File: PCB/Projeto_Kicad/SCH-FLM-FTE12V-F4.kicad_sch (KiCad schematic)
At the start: 19 parts, among them J1 BPSC-4, J2 MCS-6, Q3 BC547, Q4 BC547, U1 ESP32-WROOM-32E-N8, U2 LM358N

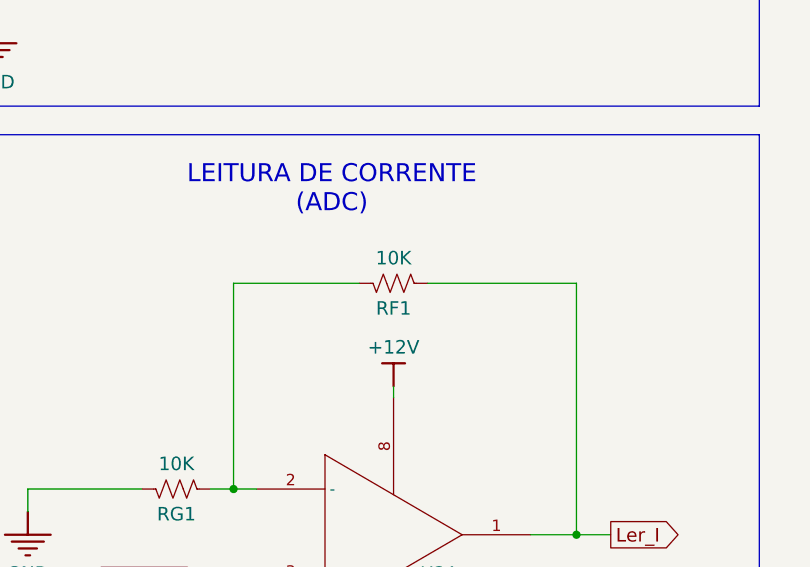
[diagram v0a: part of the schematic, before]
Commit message: Adição do R7 em paralelo com R6 e adição do RF2 de 15K e mudança de valor do RF1 de 10K para 15K
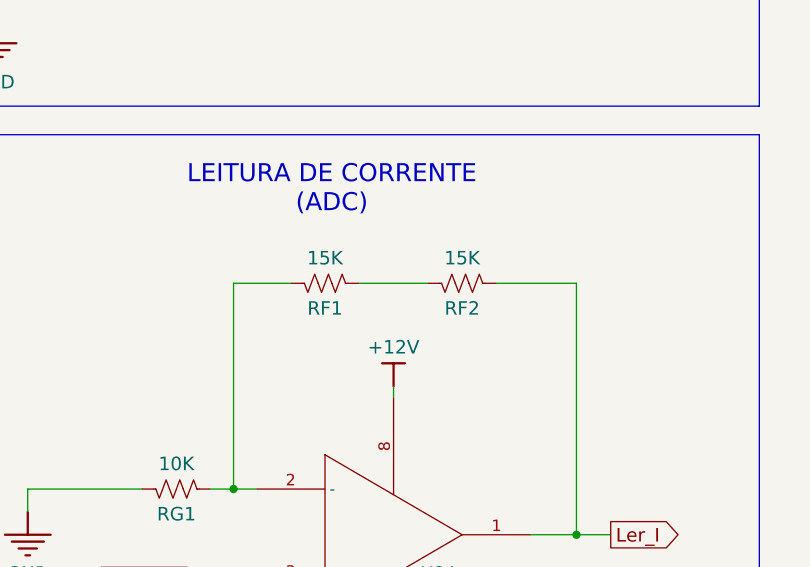
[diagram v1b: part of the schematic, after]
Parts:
- added RF2: 15K, Resistor_THT:R_Axial_DIN0207_L6.3mm_D2.5mm_P2.54mm_Vertical, symbol Device:R_US
- RF1: value 10K -> 15K
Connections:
- net Ler_I: now also RF2.2; no longer RF1.2
- new net: RF1.2, RF2.1
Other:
- moved on the sheet: RF1
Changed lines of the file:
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@@
+	(wire
+		(pts
+			(xy 120.65 227.33) (xy 129.54 227.33)
+		)
+		(stroke
+			(width 0)
+			(type default)
+		)
+	)
 	(wire
 		(pts
@@
 	(wire
 		(pts
-			(xy 105.41 227.33) (xy 91.44 227.33)
+			(xy 97.79 227.33) (xy 91.44 227.33)
 		)
 		(stroke
@@
 	(wire
 		(pts
-			(xy 113.03 227.33) (xy 129.54 227.33)
-		)
-		(stroke
-			(width 0)
-			(type default)
-		)
-	)
-	(wire
-		(pts
 			(xy 81.28 250.19) (xy 68.58 250.19)
 		)
@@
 		(pts
 			(xy 55.88 58.42) (xy 69.85 58.42)
+		)
+		(stroke
+			(width 0)
+			(type default)
+		)
+	)
+	(wire
+		(pts
+			(xy 105.41 227.33) (xy 113.03 227.33)
 		)
 		(stroke
@@
 				(path "/24c863d3-5da9-46c2-adf2-885da2a6f9d5/d196a6d6-d89b-4d92-bbb9-3bc0a8b87648"
 					(reference "R9")
+					(unit 1)
+				)
+			)
+		)
+	)
+	(symbol
+		(lib_id "Device:R_US")
+		(at 116.84 227.33 90)
+		(mirror x)
+		(unit 1)
+		(body_style 1)
+		(exclude_from_sim no)
+		(in_bom yes)
+		(on_board yes)
+		(in_pos_files yes)
+		(dnp no)
+		(property "Reference" "RF2"
+			(at 116.84 230.124 90)
+			(show_name no)
+			(do_not_autoplace no)
+			(effects
+				(font
+					(size 1.5 1.5)
+				)
+			)
+		)
+		(property "Value" "15K"
+			(at 116.84 224.536 90)
+			(show_name no)
+			(do_not_autoplace no)
+			(effects
+				(font
+					(size 1.5 1.5)
+				)
+			)
+		)
+		(property "Footprint" "Resistor_THT:R_Axial_DIN0207_L6.3mm_D2.5mm_P2.54mm_Vertical"
+			(at 117.094 228.346 90)
+			(hide yes)
+			(show_name no)
+			(do_not_autoplace no)
+			(effects
+				(font
+					(size 1.27 1.27)
+				)
+			)
+		)
+		(property "Datasheet" ""
+			(at 116.84 227.33 0)
+			(hide yes)
+			(show_name no)
+			(do_not_autoplace no)
+			(effects
+				(font
+					(size 1.27 1.27)
+				)
+			)
+		)
+		(property "Description" "Resistor, US symbol"
+			(at 116.84 227.33 0)
+			(hide yes)
+			(show_name no)
+			(do_not_autoplace no)
+			(effects
+				(font
+					(size 1.27 1.27)
+				)
+			)
+		)
+		(pin "1"
+		)
+		(pin "2"
+		)
+		(instances
+			(project "PCB-FLM-FTE-12V"
+				(path "/24c863d3-5da9-46c2-adf2-885da2a6f9d5/d196a6d6-d89b-4d92-bbb9-3bc0a8b87648"
+					(reference "RF2")
 					(unit 1)
 				)
@@
 	(symbol
 		(lib_id "Device:R_US")
-		(at 109.22 227.33 90)
+		(at 101.6 227.33 90)
 		(mirror x)
 		(unit 1)
@@
 		(dnp no)
 		(property "Reference" "RF1"
-			(at 109.22 230.124 90)
+			(at 101.6 230.124 90)
 			(show_name no)
 			(do_not_autoplace no)
@@
 			)
 		)
-		(property "Value" "10K"
-			(at 109.22 224.536 90)
+		(property "Value" "15K"
+			(at 101.6 224.536 90)
 			(show_name no)
 			(do_not_autoplace no)
@@
 		)
 		(property "Footprint" "Resistor_THT:R_Axial_DIN0207_L6.3mm_D2.5mm_P2.54mm_Vertical"
-			(at 109.474 228.346 90)
+			(at 101.854 228.346 90)
 			(hide yes)
 			(show_name no)
@@
 		)
 		(property "Datasheet" ""
-			(at 109.22 227.33 0)
+			(at 101.6 227.33 0)
 			(hide yes)
 			(show_name no)
@@
 		)
 		(property "Description" "Resistor, US symbol"
-			(at 109.22 227.33 0)
-			(hide yes)
-			(show_name no)
+			(at 101.6 227.33 0)
+			(hide yes)
+			(show_name no)
